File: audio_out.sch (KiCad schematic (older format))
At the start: 14 parts, among them U16 TL084

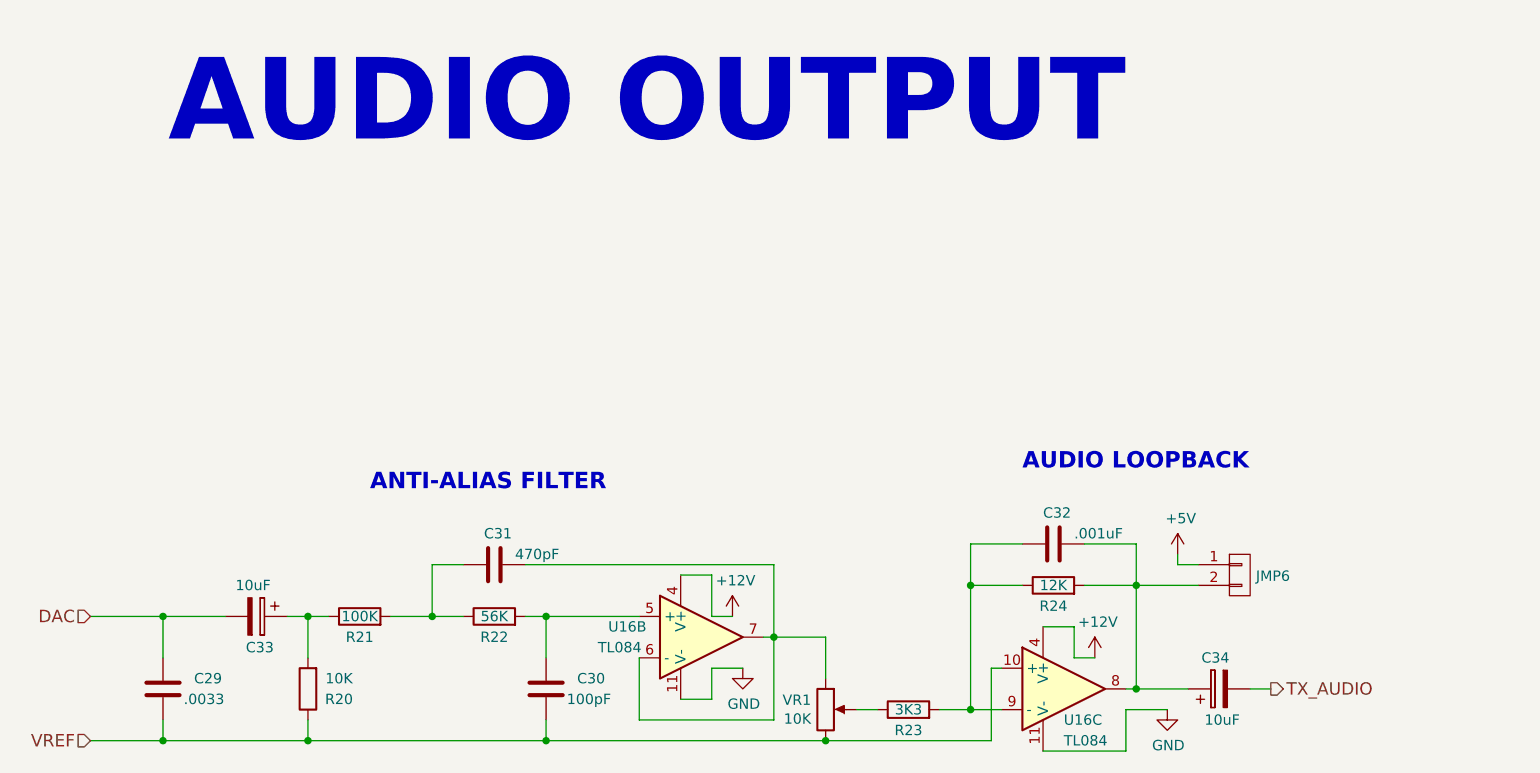
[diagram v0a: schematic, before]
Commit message: Final parts placement and verified net against an actual Issue 3 board.
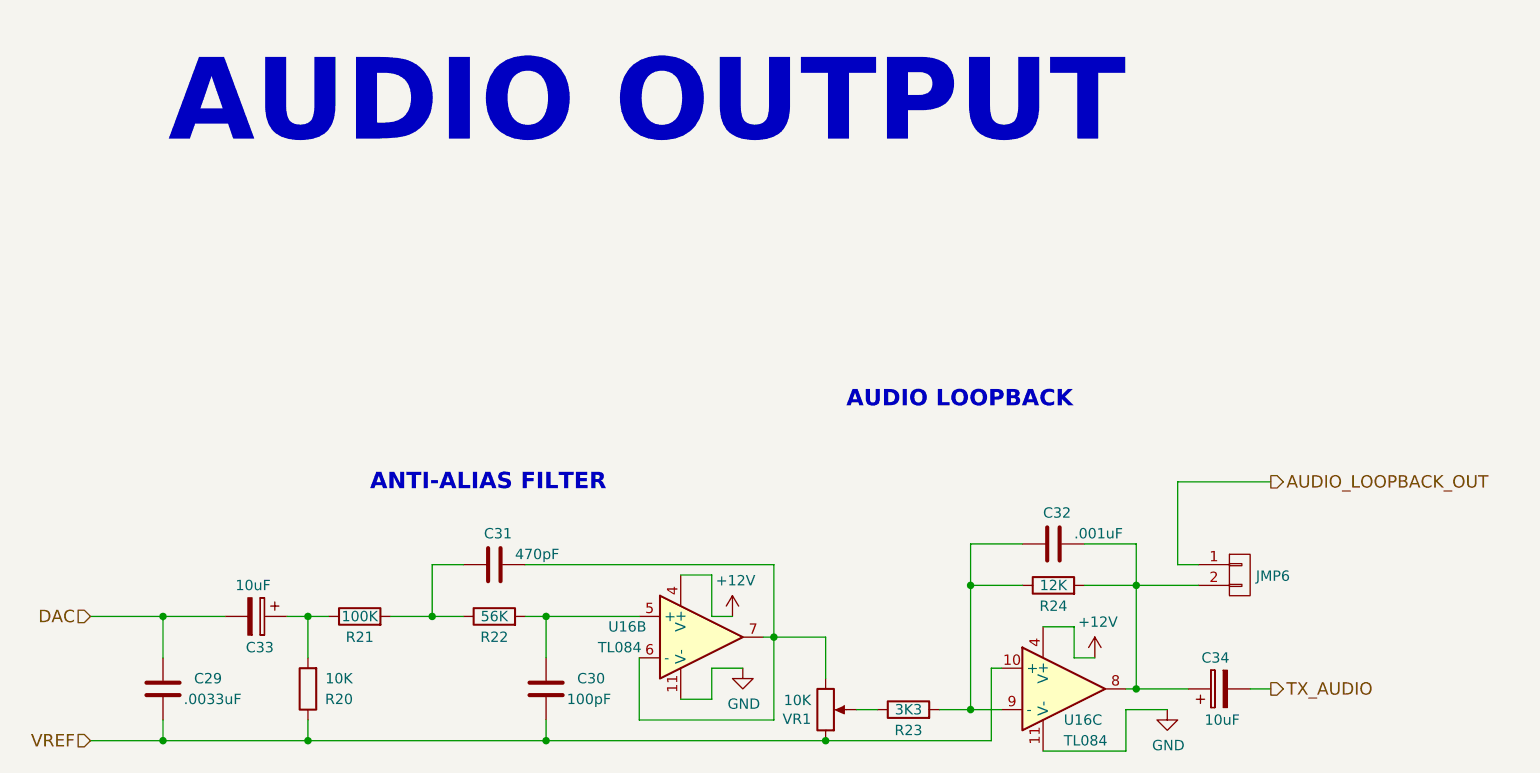
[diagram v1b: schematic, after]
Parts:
- C29: value .0033 -> .0033uF
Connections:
- net VREF: now also VR1.1; no longer VR1.3
- net at C31.1, U16.6 (-), U16.7: now also VR1.3; no longer VR1.1
- net +5V renamed AUDIO_LOOPBACK_OUT
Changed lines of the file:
@@
 	6200 4000 6100 4000
 Connection ~ 3450 4600
-Text Notes 7600 3300 0    79   ~ 16
+Text Notes 6750 3000 0    79   ~ 16
 AUDIO LOOPBACK
 Wire Wire Line
@@
 P 3450 4350
 F 0 "C29" H 3600 4400 50  0000 L CNN
-F 1 ".0033" H 3550 4300 50  0000 L CNN
+F 1 ".0033uF" H 3550 4300 50  0000 L CNN
 F 2 "Capacitors_THT:C_Axial_L3.8mm_D2.6mm_P10.00mm_Horizontal" H 3488 4200 50  0001 C CNN
 F 3 "" H 3450 4350 50  0001 C CNN
@@
 F 3 "https://www.bourns.com/pdfs/3296.pdf" H 6650 4450 50  0001 C CNN
 	1    6650 4450
-	1    0    0    -1
+	1    0    0    1
 $EndComp
 Wire Wire Line
@@
 $EndComp
 Wire Wire Line
-	8350 3750 8350 3700
-Wire Wire Line
-	8450 3750 8350 3750
+	8350 3350 8350 3750
+Wire Wire Line
+	8350 3750 8450 3750
 Wire Wire Line
 	8700 4350 8800 4350
@@
 Wire Wire Line
 	8100 4350 8400 4350
-$Comp
-L +5V #PWR057
-U 1 1 59858769
-P 8350 3700
-F 0 "#PWR057" H 8350 3550 50  0001 C CNN
-F 1 "+5V" H 8365 3873 50  0000 C CNN
-F 2 "" H 8350 3700 50  0001 C CNN
-F 3 "" H 8350 3700 50  0001 C CNN
-	1    8350 3700
-	1    0    0    -1
-$EndComp
 $Comp
 L CONN_01X02 JMP6
@@
 Text Notes 8100 1750 2    394  ~ 79
 AUDIO OUTPUT
+Text HLabel 8800 3350 2    60   Output ~ 0
+AUDIO_LOOPBACK_OUT
+Wire Wire Line
+	8800 3350 8350 3350
 $EndSCHEMATC
